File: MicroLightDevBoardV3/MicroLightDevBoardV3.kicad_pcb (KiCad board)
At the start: 6 copper layers, 12.5 x 16 mm, 33 parts, among them J1 TYPE-C-31-M-12, J3 Conn_01x03_Socket, J4 Conn_01x01_Socket, J5 Conn_01x01_Socket, J6 Conn_01x04_Socket, SW1 SW_Push, U1 USBLC6-2P6, U2 STM32C071GBUx, U3 BQ25180, U4 S-85S1AB33-I6T1U, U7 MC3479

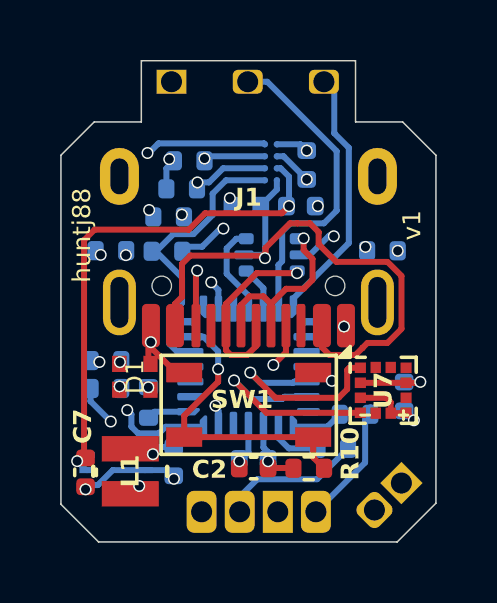
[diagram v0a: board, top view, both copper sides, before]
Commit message: pcb: optimize routing a bit
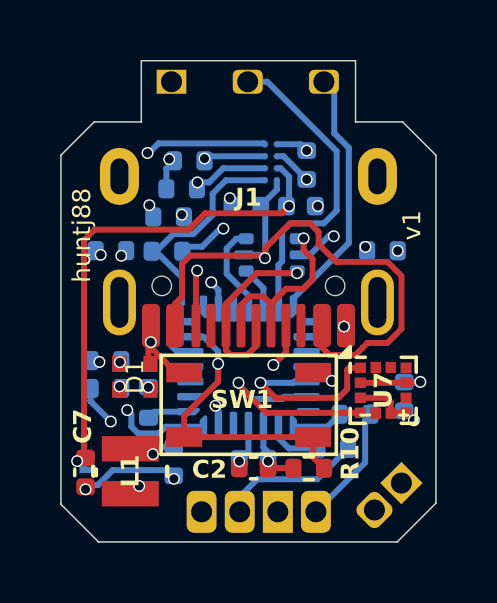
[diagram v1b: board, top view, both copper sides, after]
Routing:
- net Net-(J6-Pin_1): track 12.6 -> 11.9 mm

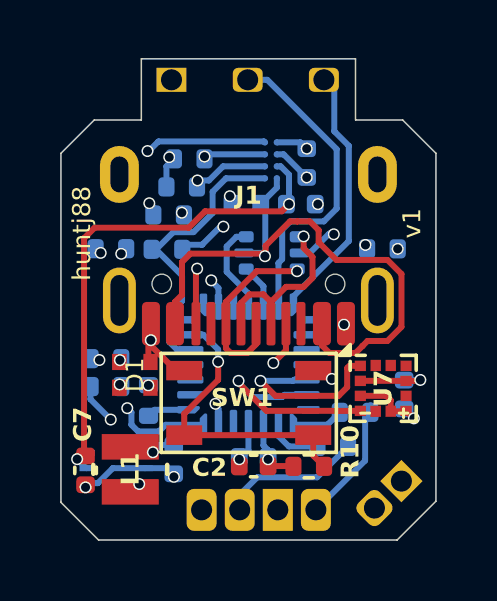
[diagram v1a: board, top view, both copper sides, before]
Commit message: pcb: optimize routing a bit
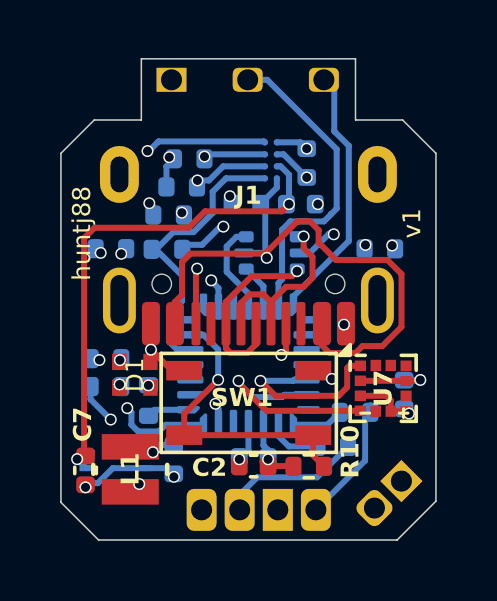
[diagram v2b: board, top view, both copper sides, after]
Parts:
- moved R2 0.09 mm to (54.1, 24.1)
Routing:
- net Net-(J1-CC1): track 8.95 -> 7.21 mm
- net GND: track 20.0 -> 20.6 mm
- net TS_MR_CHRG: track 22.4 -> 23.0 mm

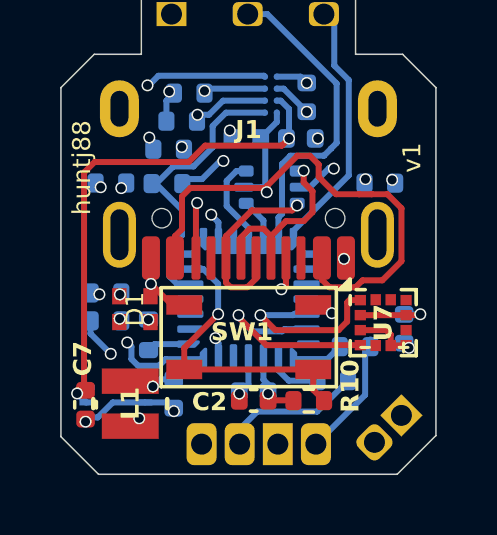
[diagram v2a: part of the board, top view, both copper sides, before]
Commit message: pcb: optimize routing a bit
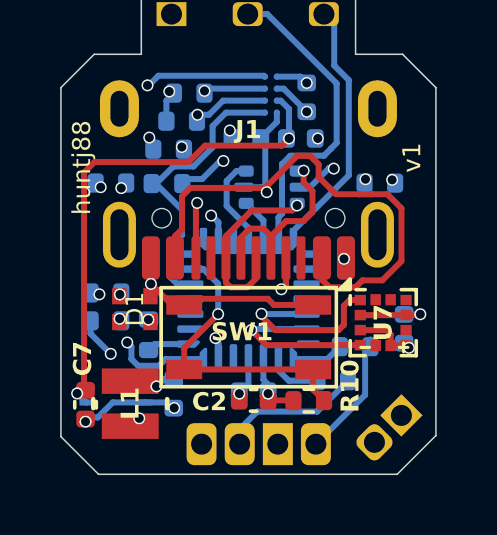
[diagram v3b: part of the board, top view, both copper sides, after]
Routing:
- net GND: track 20.6 -> 24.6 mm, vias 13 -> 12
- net I2C_SDA: track 17.9 -> 17.2 mm

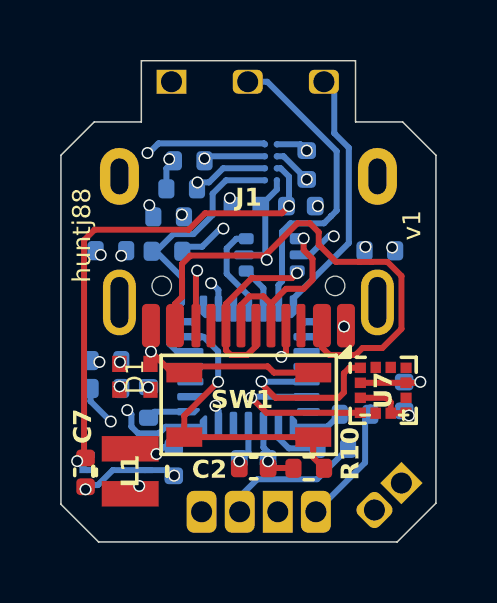
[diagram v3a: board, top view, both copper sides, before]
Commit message: pcb: optimize routing
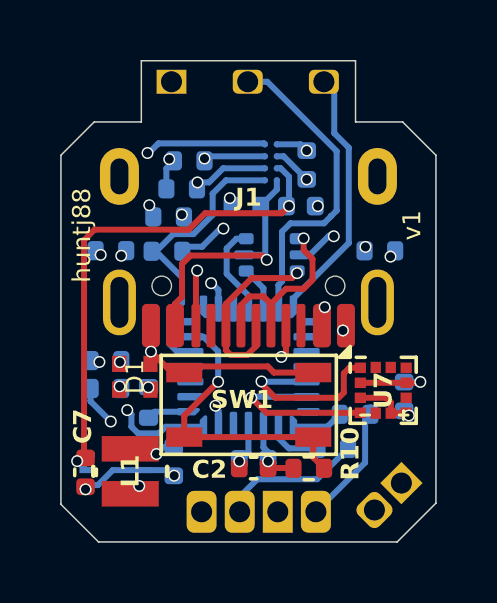
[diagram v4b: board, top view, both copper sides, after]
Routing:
- net VBUS_CHRG: track 20.6 -> 16.6 mm, vias 1 -> 2
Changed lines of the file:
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@@
-	)
-	(segment
-		(start 50.36 24.385)
-		(end 50.37 24.375)
-		(width 0.2)
-		(layer "F.Cu")
-		(net 1)
 	)
 	(segment
@@
 	)
 	(segment
-		(start 53.442479 24.456)
-		(end 53.857521 24.456)
-		(width 0.2)
-		(layer "F.Cu")
-		(net 1)
-	)
-	(segment
 		(start 47.816 24.244)
 		(end 47.535 24.525)
@@
 	)
 	(segment
-		(start 54.212529 27.325256)
-		(end 53.551 27.325256)
-		(width 0.2)
-		(layer "F.Cu")
-		(net 1)
-	)
-	(segment
-		(start 53.857521 24.456)
-		(end 53.859521 24.454)
-		(width 0.2)
-		(layer "F.Cu")
-		(net 1)
-	)
-	(segment
-		(start 54.381785 24.454)
-		(end 54.851 24.923215)
-		(width 0.2)
-		(layer "F.Cu")
-		(net 1)
-	)
-	(segment
-		(start 52.091 23.462479)
-		(end 52.091 23.877521)
-		(width 0.2)
-		(layer "F.Cu")
-		(net 1)
-	)
-	(segment
-		(start 52.091 23.877521)
-		(end 52.667479 24.454)
-		(width 0.2)
-		(layer "F.Cu")
-		(net 1)
-	)
-	(segment
 		(start 50.265 24.295)
 		(end 50.214 24.244)
@@
 	)
 	(segment
-		(start 50.37 24.375)
-		(end 50.37 24.181479)
-		(width 0.2)
-		(layer "F.Cu")
-		(net 1)
-	)
-	(segment
 		(start 50.36 24.385)
 		(end 50.27 24.295)
@@
 	)
 	(segment
-		(start 51.797521 23.169)
-		(end 52.091 23.462479)
-		(width 0.2)
-		(layer "F.Cu")
-		(net 1)
-	)
-	(segment
-		(start 52.2 27.304999)
+		(start 52.29 25.965)
+		(end 52.22 25.965)
+		(width 0.2)
+		(layer "F.Cu")
+		(net 1)
+	)
+	(segment
+		(start 52.2 25.985)
 		(end 52.2 26.58)
-		(width 0.2)
-		(layer "F.Cu")
-		(net 1)
-	)
-	(segment
-		(start 52.451001 27.556)
-		(end 52.2 27.304999)
-		(width 0.2)
-		(layer "F.Cu")
-		(net 1)
-	)
-	(segment
-		(start 53.551 27.325256)
-		(end 53.320256 27.556)
-		(width 0.2)
-		(layer "F.Cu")
-		(net 1)
-	)
-	(segment
-		(start 52.667479 24.454)
-		(end 53.440479 24.454)
-		(width 0.2)
-		(layer "F.Cu")
-		(net 1)
-	)
-	(segment
-		(start 53.320256 27.556)
-		(end 52.451001 27.556)
 		(width 0.2)
 		(layer "F.Cu")
@@
 	)
 	(segment
-		(start 50.37 24.181479)
-		(end 51.382479 23.169)
-		(width 0.2)
-		(layer "F.Cu")
-		(net 1)
-	)
-	(segment
-		(start 54.851 26.686785)
-		(end 54.212529 27.325256)
-		(width 0.2)
-		(layer "F.Cu")
-		(net 1)
-	)
-	(segment
-		(start 54.851 24.923215)
-		(end 54.851 26.686785)
-		(width 0.2)
-		(layer "F.Cu")
-		(net 1)
-	)
-	(segment
-		(start 51.382479 23.169)
-		(end 51.797521 23.169)
-		(width 0.2)
-		(layer "F.Cu")
-		(net 1)
-	)
-	(segment
 		(start 47.3 25.855001)
 		(end 47.3 26.58)
@@
 	)
 	(segment
-		(start 53.440479 24.454)
-		(end 53.442479 24.456)
-		(width 0.2)
-		(layer "F.Cu")
-		(net 1)
-	)
-	(segment
-		(start 53.859521 24.454)
-		(end 54.381785 24.454)
-		(width 0.2)
-		(layer "F.Cu")
+		(start 52.22 25.965)
+		(end 52.2 25.985)
+		(width 0.2)
+		(layer "F.Cu")
+		(net 1)
+	)
+	(via
+		(at 52.29 25.965)
+		(size 0.4)
+		(drill 0.3)
+		(layers "F.Cu" "B.Cu")
 		(net 1)
 	)
@@
 	)
 	(segment
+		(start 50.639979 28.1235)
+		(end 50.3465 27.830021)
+		(width 0.2)
+		(layer "In2.Cu")
+		(net 1)
+	)
+	(segment
+		(start 52.09 26.165)
+		(end 52.09 27.088521)
+		(width 0.2)
+		(layer "In2.Cu")
+		(net 1)
+	)
+	(segment
+		(start 50.3465 27.830021)
+		(end 50.3465 24.3985)
+		(width 0.2)
+		(layer "In2.Cu")
+		(net 1)
+	)
+	(segment
+		(start 52.09 27.088521)
+		(end 51.055021 28.1235)
+		(width 0.2)
+		(layer "In2.Cu")
+		(net 1)
+	)
+	(segment
+		(start 52.29 25.965)
+		(end 52.09 26.165)
+		(width 0.2)
+		(layer "In2.Cu")
+		(net 1)
+	)
+	(segment
+		(start 50.3465 24.3985)
+		(end 50.36 24.385)
+		(width 0.2)
+		(layer "In2.Cu")
+		(net 1)
+	)
+	(segment
+		(start 51.055021 28.1235)
+		(end 50.639979 28.1235)
+		(width 0.2)
+		(layer "In2.Cu")
+		(net 1)
+	)
+	(segment
 		(start 46.484997 27.460003)
 		(end 46.5 27.445)
@@
 	)
 	(via
-		(at 52.935 26.61)
+		(at 52.9 26.74)
 		(size 0.4)
 		(drill 0.3)
@@
 	)
 	(segment
-		(start 53.890437 29.336042)
-		(end 53.890437 32.665437)
-		(width 0.2)
-		(layer "In2.Cu")
-		(net 4)
-	)
-	(segment
-		(start 53.483521 23.17)
-		(end 54.51852 23.17)
+		(start 54.70352 23.355)
+		(end 55.23 23.88148)
 		(width 0.2)
 		(layer "In2.Cu")
@@
 	)
 	(segment
-		(start 55.045 28.181479)
-		(end 53.890437 29.336042)
+		(start 53.668521 23.355)
+		(end 54.70352 23.355)
 		(width 0.2)
 		(layer "In2.Cu")
@@
 	)
 	(segment
-		(start 54.51852 23.17)
-		(end 55.045 23.69648)
+		(start 53.890437 28.524563)
+		(end 53.890437 32.665437)
+		(width 0.2)
+		(layer "In2.Cu")
+		(net 4)
+	)
+	(segment
+		(start 52.018519 21.704998)
+		(end 53.668521 23.355)
 		(width 0.2)
 		(layer "In2.Cu")
@@
 	)
 	(segment
-		(start 55.045 23.69648)
-		(end 55.045 28.181479)
+		(start 55.23 27.185)
+		(end 53.890437 28.524563)
 		(width 0.2)
 		(layer "In2.Cu")
@@
 	)
 	(segment
-		(start 52.018519 21.704998)
-		(end 53.483521 23.17)
+		(start 55.23 23.88148)
+		(end 55.23 27.185)
 		(width 0.2)
 		(layer "In2.Cu")
@@
 	)
 	(via
-		(at 54.54 23.975)
+		(at 54.485 24.28)
 		(size 0.4)
 		(drill 0.3)
@@
 	)
 	(segment
-		(start 54.54 23.975)
-		(end 54.06 24.455)
-		(width 0.2)
-		(layer "In2.Cu")
+		(start 54.64 24.085001)
+		(end 54.64 24.125)
+		(width 0.2)
+		(layer "B.Cu")
 		(net 17)
 	)
 	(segment
-		(start 54.06 24.455)
-		(end 53.756 24.455)
+		(start 54.64 24.125)
+		(end 54.485 24.28)
+		(width 0.2)
+		(layer "B.Cu")
+		(net 17)
+	)
+	(segment
+		(start 54.033521 24.28)
+		(end 53.857521 24.456)
+		(width 0.2)
+		(layer "In2.Cu")
+		(net 17)
+	)
+	(segment
+		(start 54.485 24.28)
+		(end 54.033521 24.28)
 		(width 0.2)
 		(layer "In2.Cu")
@@
 	)
 	(segment
-		(start 53.756 24.455)
-		(end 53.755 24.456)
-		(width 0.2)
-		(layer "In2.Cu")
-		(net 17)
-	)
-	(segment
 		(start 52.481992 24.456)
 		(end 50.8475 26.090492)
@@
 	)
 	(segment
-		(start 53.755 24.456)
+		(start 53.857521 24.456)
 		(end 52.481992 24.456)
 		(width 0.2)

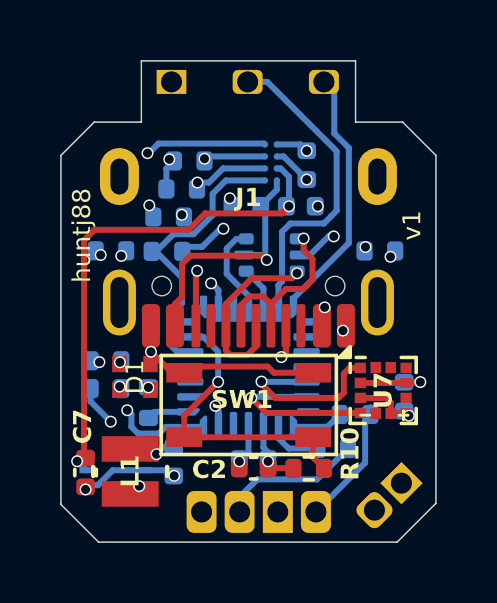
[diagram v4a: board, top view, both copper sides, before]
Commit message: pcb: edge cut cleanup, optimize routing
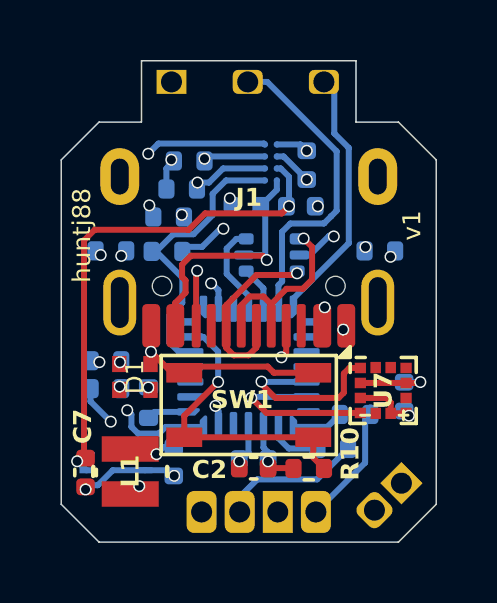
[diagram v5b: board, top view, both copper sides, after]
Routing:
- net Net-(J1-D--PadA7): track 6.08 -> 6.76 mm
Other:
- outline, holes or cut-outs redrawn

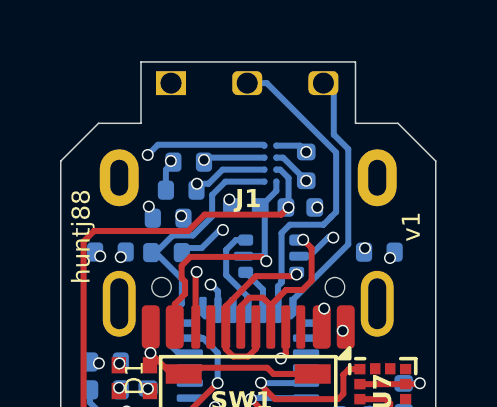
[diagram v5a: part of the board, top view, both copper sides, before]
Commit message: extend debug pins slightly further from usb, add production files to git
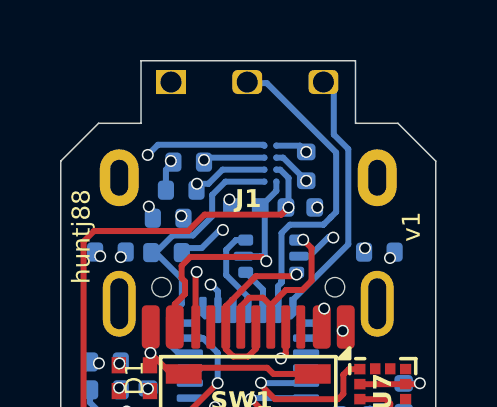
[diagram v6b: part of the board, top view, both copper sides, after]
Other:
- board size 12.5 x 16 mm -> 12.5 x 16.1 mm
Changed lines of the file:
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@@
 	(footprint "MicroLightDevBoard:Microlight_debug_pins"
 		(layer "F.Cu")
-		(at 47.185 18.45 90)
+		(at 47.185 18.415 90)
 		(descr "Through hole straight socket strip, 1x03, 2.54mm pitch, single row (from Kicad 4.0.7), script generated")
 		(tags "Through hole socket strip THT 1x03 2.54mm single row")
@@
 	)
 	(gr_line
-		(start 54.750003 19.789995)
-		(end 56.00981 21.049807)
+		(start 46.185 17.705)
+		(end 46.185 19.79)
 		(stroke
 			(width 0.05)
 			(type default)
 		)
-		(locked yes)
 		(layer "Edge.Cuts")
 	)
 	(gr_line
-		(start 53.33462 17.749995)
-		(end 53.33462 19.789995)
+		(start 54.750003 19.789995)
+		(end 56.00981 21.049807)
 		(stroke
 			(width 0.05)
@@
 	)
 	(gr_line
-		(start 46.185 17.745)
-		(end 46.185 19.785)
-		(stroke
-			(width 0.05)
-			(type default)
-		)
-		(locked yes)
-		(layer "Edge.Cuts")
-	)
-	(gr_line
 		(start 44.769617 19.79)
 		(end 43.509807 21.049807)
@@
 	)
 	(gr_line
-		(start 46.185 17.745)
-		(end 53.33462 17.745)
+		(start 53.33462 17.705)
+		(end 53.33462 19.789995)
+		(stroke
+			(width 0.05)
+			(type default)
+		)
+		(layer "Edge.Cuts")
+	)
+	(gr_line
+		(start 46.185 17.705)
+		(end 53.33462 17.705)
 		(stroke
 			(width 0.05)

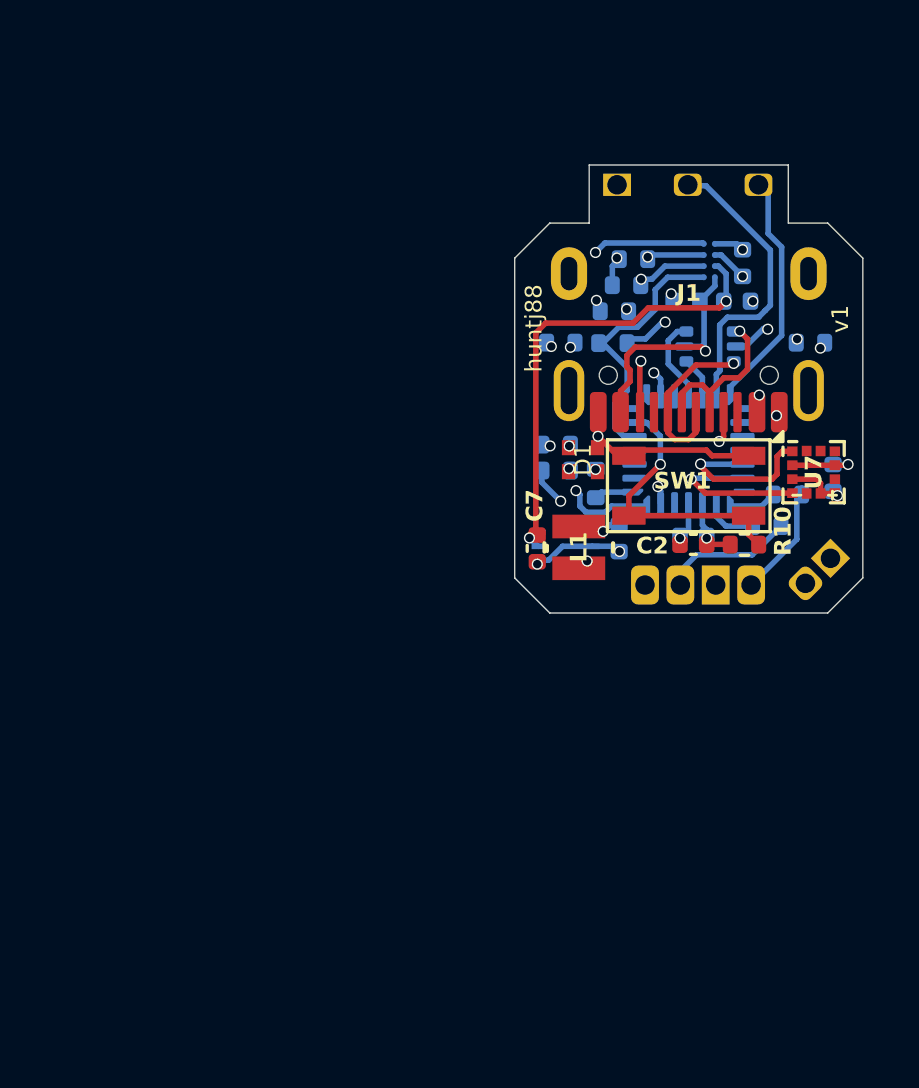
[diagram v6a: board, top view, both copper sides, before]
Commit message: PCB edge cuts routing and v-cut (#20)
* edge cuts / panelization technique

* add horizontal v-cut
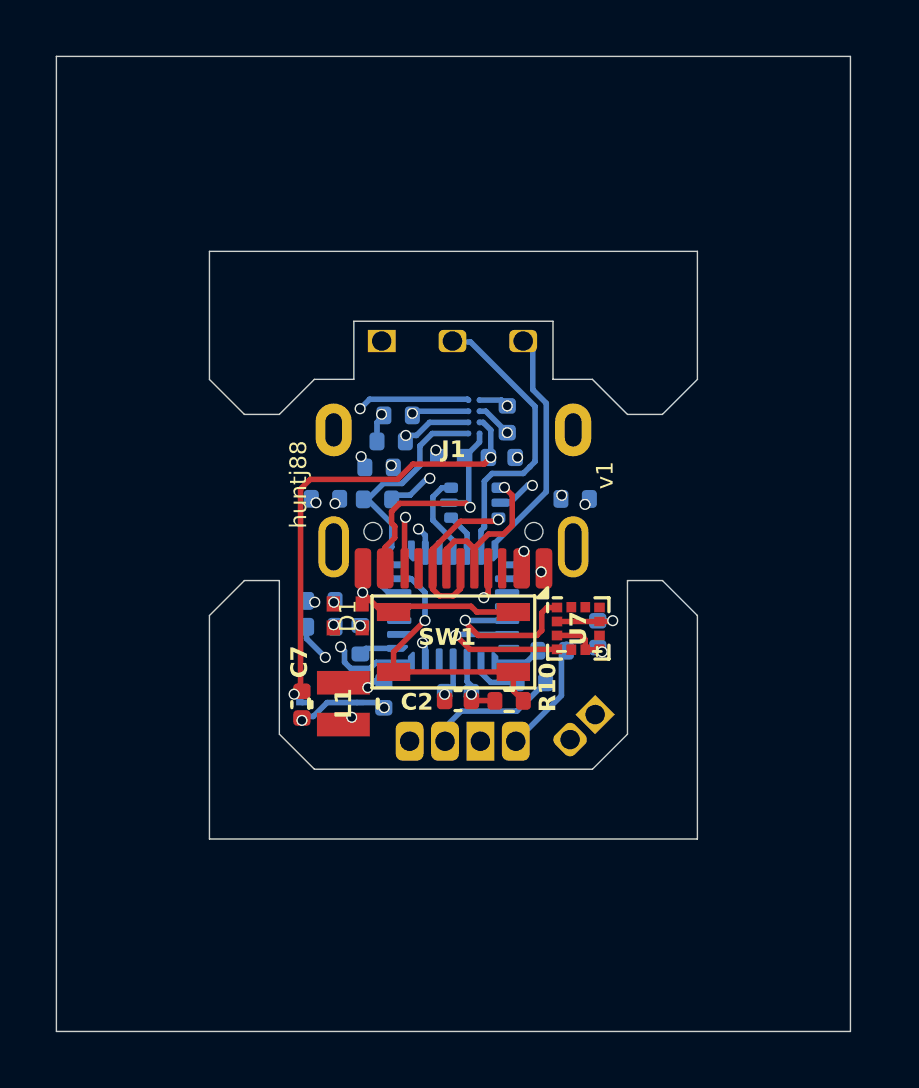
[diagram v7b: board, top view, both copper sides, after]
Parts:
- moved D1 10.1 mm to (37.5, 33.9)
- moved L1 10.1 mm to (37.4, 37.0)
- moved R11 10.1 mm to (44.9, 35.1)
- moved R3 10.1 mm to (38.6, 28.6)
- moved U2 10.1 mm to (41.3, 33.6)
- moved U4 10.1 mm to (36.9, 37.0)
- moved C3 10.1 mm to (41.2, 28.2)
- moved C7 10.1 mm to (35.9, 37.1)
- moved J3 10.1 mm to (38.7, 24.0)
- moved J4 10.1 mm to (45.5, 38.3)
- moved R12 10.1 mm to (44.1, 36.3)
- moved R2 10.1 mm to (45.7, 29.7)
- moved R8 10.1 mm to (38.0, 34.8)
- moved U7 10.1 mm to (45.8, 34.3)
- moved J6 10.1 mm to (39.7, 38.4)
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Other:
- board size 12.5 x 16.1 mm -> 28.5 x 35 mm
- board text added: "V-cut"

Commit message: update button pullup resistor value to value I (accidentally) actually used, it worked
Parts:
- R10: value 6.8k -> 10k
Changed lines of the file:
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@@
 			)
 		)
-		(property "Value" "6.8k"
+		(property "Value" "10k"
 			(at 0 1.17 0)
 			(layer "F.Fab")
@@
 					(thickness 0.15)
 				)
-				(justify mirror)
-			)
-		)
-		(property "LSCS" "C7070110"
-			(at 0 0 180)
-			(unlocked yes)
-			(layer "B.Fab")
-			(hide yes)
-			(effects
-				(font
-					(size 1 1)
-					(thickness 0.15)
-				)
